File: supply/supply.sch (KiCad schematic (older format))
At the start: 35 parts

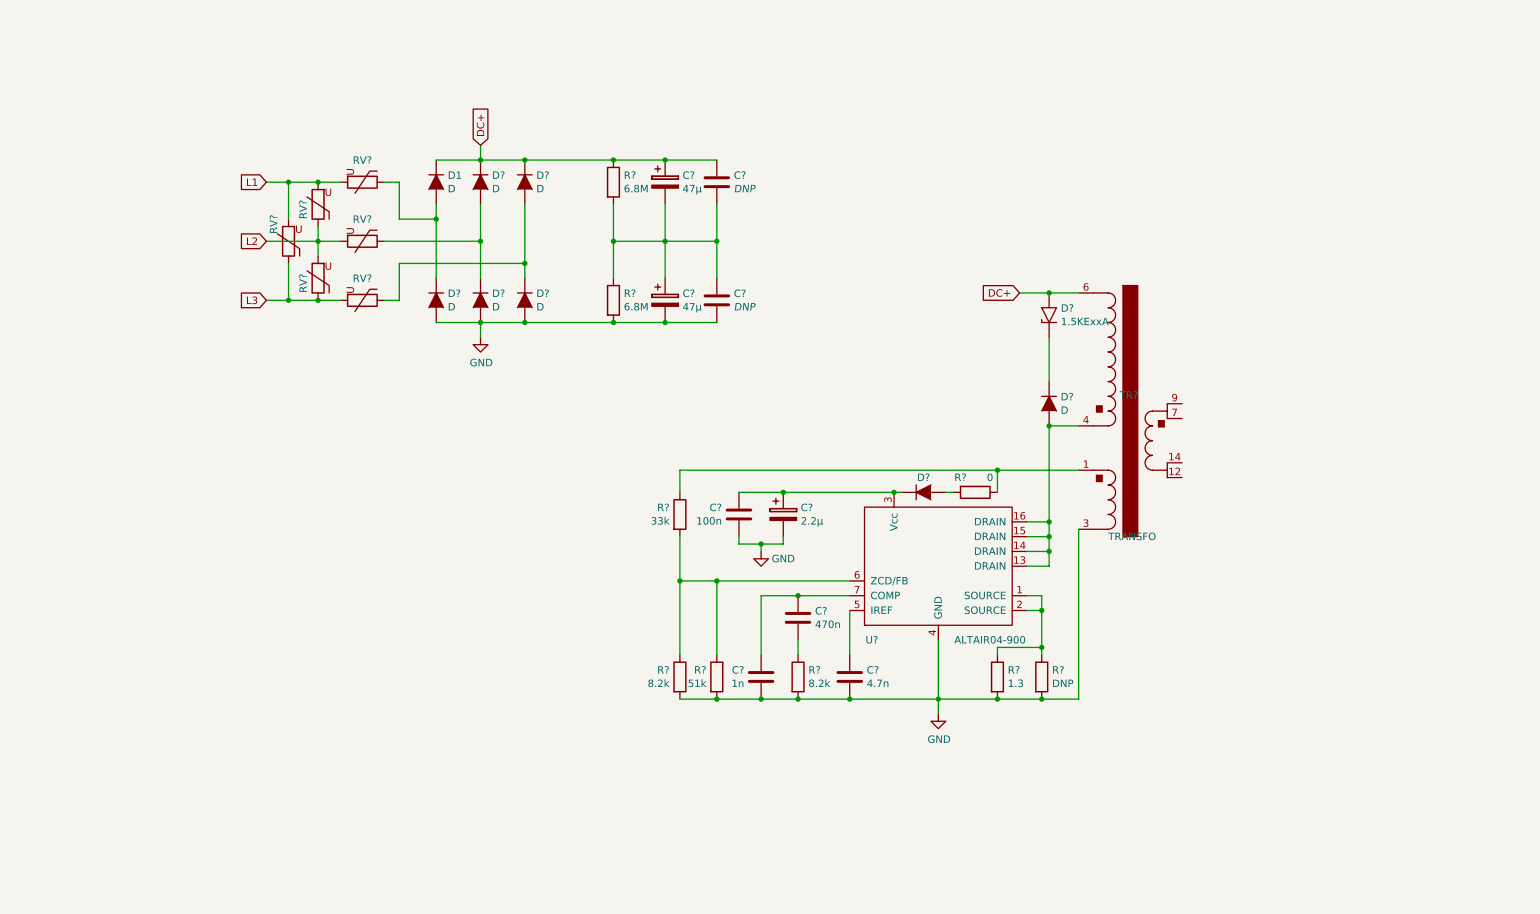
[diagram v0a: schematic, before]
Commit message: Add Li charger/protection
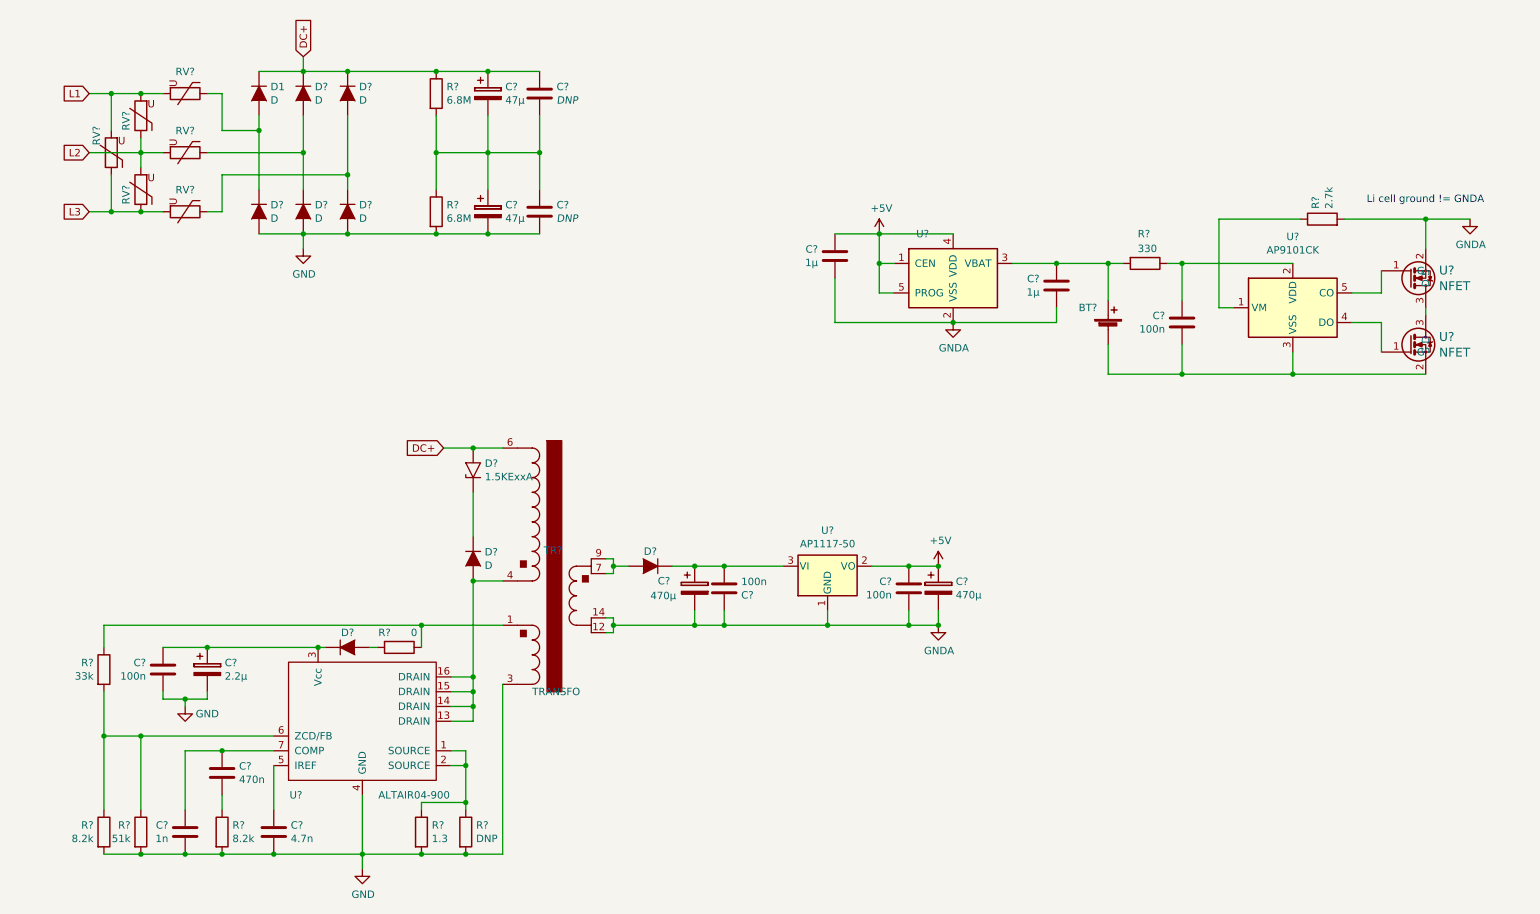
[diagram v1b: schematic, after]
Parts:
- added BT?: Battery_Cell, symbol Device:Battery_Cell
- added C? (x2): 470µ, symbol stmbl:CP
- added C? (x3): 100n, stmbl:C_0805, symbol stmbl:C
- added C? (x2): 1µ, stmbl:C_0805, symbol stmbl:C
- added D?: D, stmbl:SMA_Standard, symbol stmbl:D
- added R?: 330, stmbl:R_0805, symbol stmbl:R
- added R?: 2.7k, stmbl:R_0805, symbol stmbl:R
- added U?: AP1117-50, Package_TO_SOT_SMD:SOT-223-3_TabPin2, symbol Regulator_Linear:AP1117-50
- added U?: MCP73811T-420I-OT, Package_TO_SOT_SMD:SOT-23-5, symbol Battery_Management:MCP73811T-420I-OT
- added U?: AP9101CK, Package_TO_SOT_SMD:SOT-23-5, symbol Battery_Management:AP9101CK
- added U? (x2): NFET, symbol stmbl:NFET
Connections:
- net GNDA: now reaches TR?.12
- net GNDA: now also TR?.14, C?.1, C?.2, C?.2, C?.2, C?.2, C?.2, R?.2, U?.1 (GND), U?.2 (S), U?.2 (VSS)
- net at TR?.7: now also TR?.9, D?.2 (A)
- new net: C?.1, C?.2, D?.1 (K), U?.3 (VI)
- new net: BT?.1 (+), C?.1, R?.2, U?.3 (VBAT)
- new net: R?.1, U?.1 (VM)
- new net: C?.1, R?.1, U?.2 (VDD)
- new net: BT?.2 (-), C?.2, U?.2 (S), U?.3 (VSS)
- new net: U?.1 (G), U?.4 (DO)
- new net: U?.1 (G), U?.5 (CO)
- new net: U?.3 (D), U?.3 (D)
- new net +5V: C?.1, C?.1, C?.1, U?.1 (CEN), U?.2 (VO), U?.4 (VDD), U?.5 (PROG)
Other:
- note added: "Li cell ground != GNDA"
- moved on the sheet: C?, D1, D?, R?, RV?, TR?, U?

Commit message: stuff
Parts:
- C10: renamed from C?; footprint (none) -> Capacitor_SMD:CP_Elec_8x10
- C14: renamed from C?; footprint (none) -> Capacitor_SMD:CP_Elec_8x10.5
- C3: renamed from C?; footprint (none) -> Capacitor_SMD:CP_Elec_6.3x3
- R7, R8: renamed from R?; footprint (none) -> stmbl:R_1206
- RV1, RV2, RV3, RV4, RV5, RV6: renamed from RV?; footprint (none) -> Varistor:RV_Disc_D12mm_W4.5mm_P7.5mm
- TR1: renamed from TR?; value TRANSFO -> 750871110; footprint (none) -> Varistor:RV_Disc_D12mm_W4.5mm_P7.5mm
- U1: renamed from U?; footprint (none) -> Package_SO:SOIC-16_3.9x9.9mm_P1.27mm
- gave numbers to parts that had none: 37
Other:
- moved on the sheet: RV1

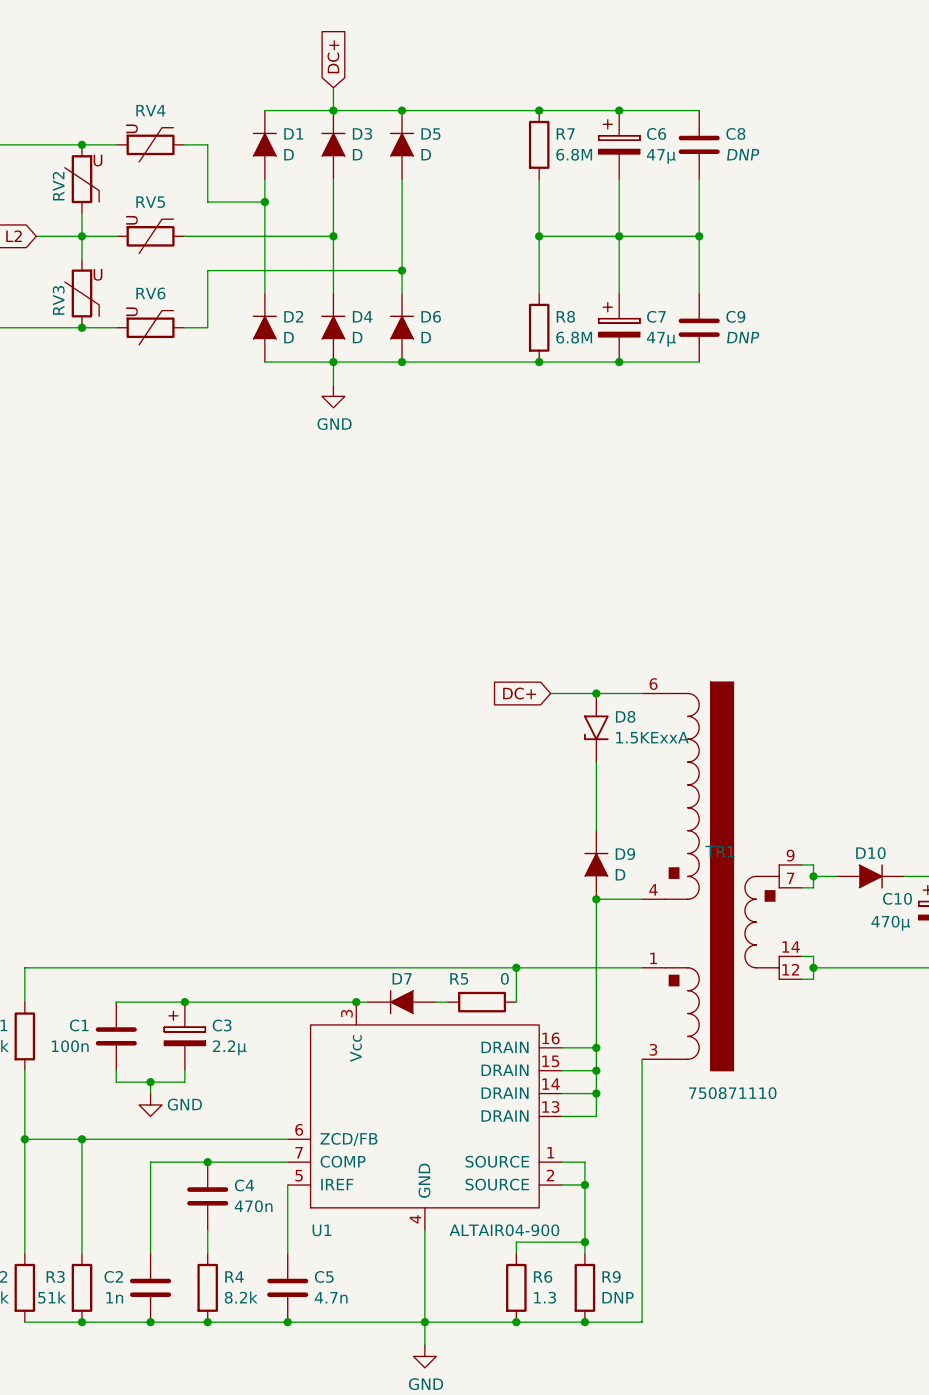
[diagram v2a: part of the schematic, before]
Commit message: add xfmr footprint
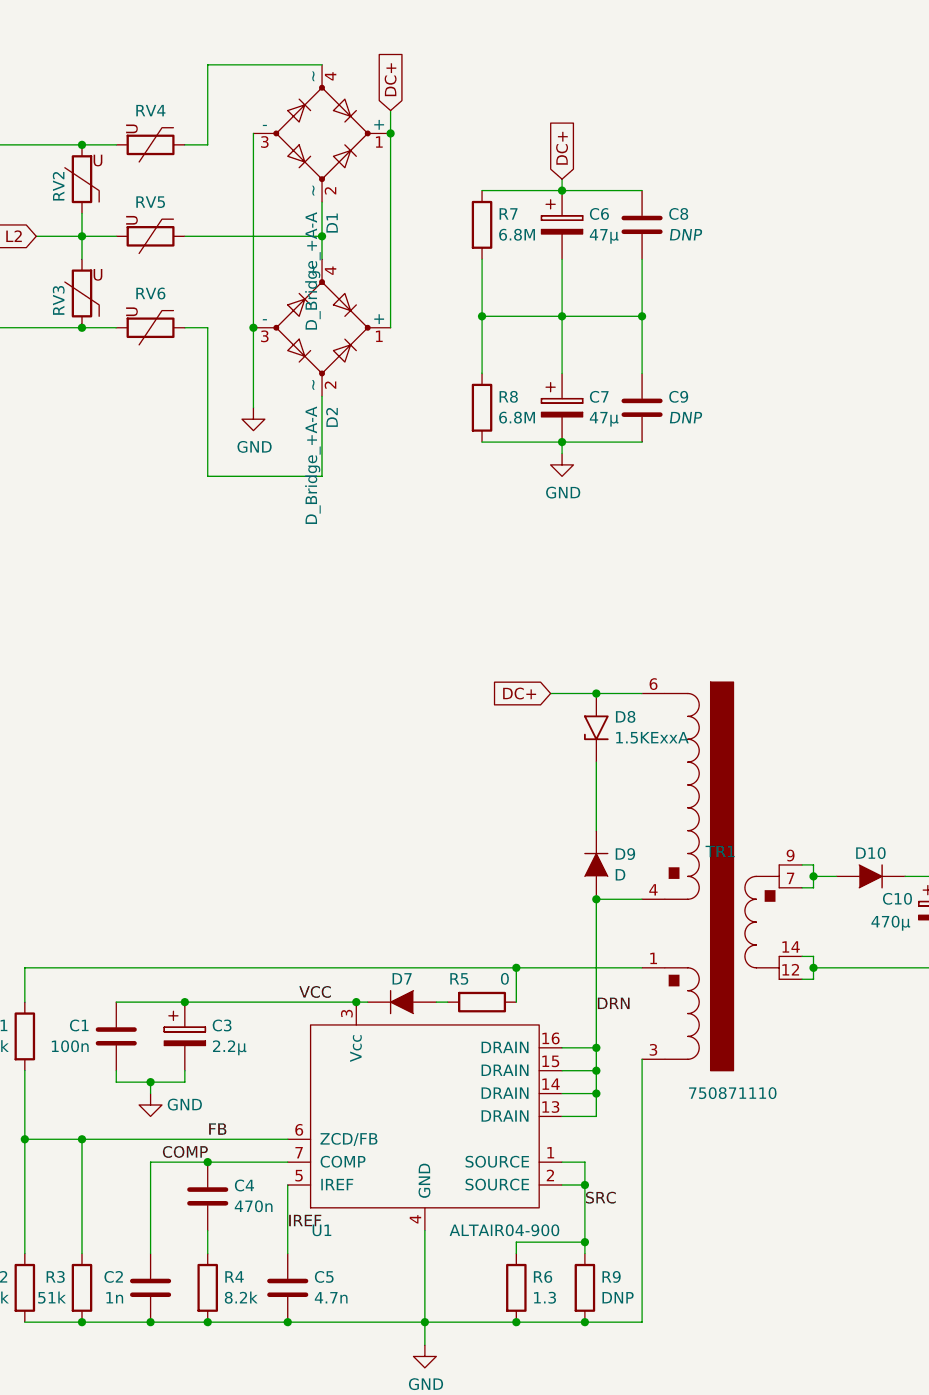
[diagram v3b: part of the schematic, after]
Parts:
- removed D1, D2, D3, D4, D5, D6: D, stmbl:SMA_Standard, symbol stmbl:D
- added D1, D2: D_Bridge_+A-A, Diodes_SMD:Diode_Bridge_MBLS, symbol Device:D_Bridge_+A-A
- C3: footprint Capacitor_SMD:CP_Elec_6.3x3 -> Capacitors_SMD:CP_Elec_6.3x4.5
- D8: footprint Diode_THT:D_DO-201AE_P15.24mm_Horizontal -> stmbl:SMA_Standard
- TR1: footprint Varistor:RV_Disc_D12mm_W4.5mm_P7.5mm -> altair04:750871110
- U5, U6: footprint (none) -> stmbl:SOT-23
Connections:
- net DC+: now also D1.1 (+), D2.1 (+)
- net GND: now also D1.3 (-), D2.3 (-)
- net at RV4.1: now also D1.4 (~~)
- net at RV5.1: now also D1.2 (~~), D2.4 (~~)
- net at RV6.1: now also D2.2 (~~)
- net SRC: now reaches R6.1, R9.1, U1.1 (SOURCE), U1.2 (SOURCE)
- net DRN: now reaches D9.2 (A), TR1.4, U1.13 (DRAIN), U1.14 (DRAIN), U1.15 (DRAIN), U1.16 (DRAIN)
- net VCC: now reaches C1.1, C3.1, D7.1 (K), U1.3 (Vcc)
- net IREF: now reaches C5.1, U1.5 (IREF)
- net FB: now reaches R1.2, R2.1, R3.1, U1.6 (ZCD/FB)
- net COMP: now reaches C2.1, C4.1, U1.7 (COMP)
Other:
- moved on the sheet: C6, C7, C8, C9, R7, R8
